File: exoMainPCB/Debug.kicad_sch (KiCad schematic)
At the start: 6 parts

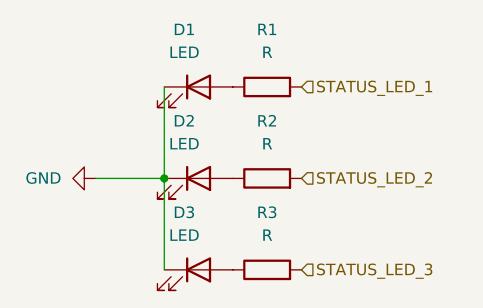
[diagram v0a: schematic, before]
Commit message: finished IMU and added component values
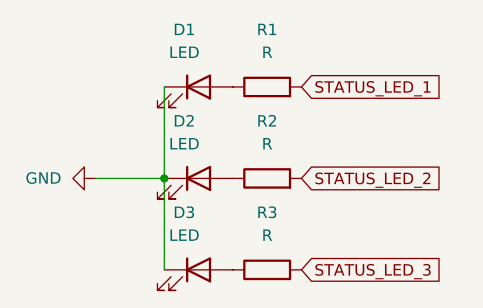
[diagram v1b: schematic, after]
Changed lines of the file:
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@@
 		)
 	)
-	(hierarchical_label "STATUS_LED_3"
+	(global_label "STATUS_LED_2"
+		(shape input)
+		(at 97.79 55.88 0)
+		(fields_autoplaced yes)
+		(effects
+			(font
+				(size 1.27 1.27)
+			)
+			(justify left)
+		)
+		(property "Intersheetrefs" "${INTERSHEET_REFS}"
+			(at 114.1403 55.88 0)
+			(effects
+				(font
+					(size 1.27 1.27)
+				)
+				(justify left)
+				(hide yes)
+			)
+		)
+	)
+	(global_label "STATUS_LED_3"
 		(shape input)
 		(at 97.79 66.04 0)
@@
 			(justify left)
 		)
+		(property "Intersheetrefs" "${INTERSHEET_REFS}"
+			(at 114.1403 66.04 0)
+			(effects
+				(font
+					(size 1.27 1.27)
+				)
+				(justify left)
+				(hide yes)
+			)
+		)
 	)
-	(hierarchical_label "STATUS_LED_1"
+	(global_label "STATUS_LED_1"
 		(shape input)
 		(at 97.79 45.72 0)
@@
 			(justify left)
 		)
-	)
-	(hierarchical_label "STATUS_LED_2"
-		(shape input)
-		(at 97.79 55.88 0)
-		(fields_autoplaced yes)
-		(effects
-			(font
-				(size 1.27 1.27)
+		(property "Intersheetrefs" "${INTERSHEET_REFS}"
+			(at 114.1403 45.72 0)
+			(effects
+				(font
+					(size 1.27 1.27)
+				)
+				(justify left)
+				(hide yes)
 			)
-			(justify left)
 		)
 	)

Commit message: changed all resistors to US, updated IO, finished Handheld
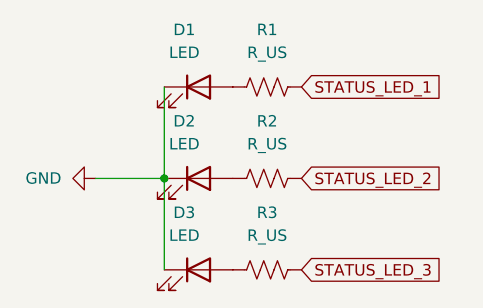
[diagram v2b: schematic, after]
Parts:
- R1, R2, R3: value R -> R_US; symbol Device:R -> Device:R_US
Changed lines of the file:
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@@
 	)
 	(symbol
-		(lib_id "Device:R")
+		(lib_id "Device:R_US")
 		(at 93.98 66.04 90)
 		(unit 1)
@@
 			)
 		)
-		(property "Value" "R"
+		(property "Value" "R_US"
 			(at 93.98 62.23 90)
 			(effects
@@
 	)
 	(symbol
-		(lib_id "Device:R")
+		(lib_id "Device:R_US")
 		(at 93.98 45.72 90)
 		(unit 1)
@@
 			)
 		)
-		(property "Value" "R"
+		(property "Value" "R_US"
 			(at 93.98 41.91 90)
 			(effects
@@
 	)
 	(symbol
-		(lib_id "Device:R")
+		(lib_id "Device:R_US")
 		(at 93.98 55.88 90)
 		(unit 1)
@@
 			)
 		)
-		(property "Value" "R"
+		(property "Value" "R_US"
 			(at 93.98 52.07 90)
 			(effects
